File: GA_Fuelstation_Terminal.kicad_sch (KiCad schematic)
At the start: 0 parts

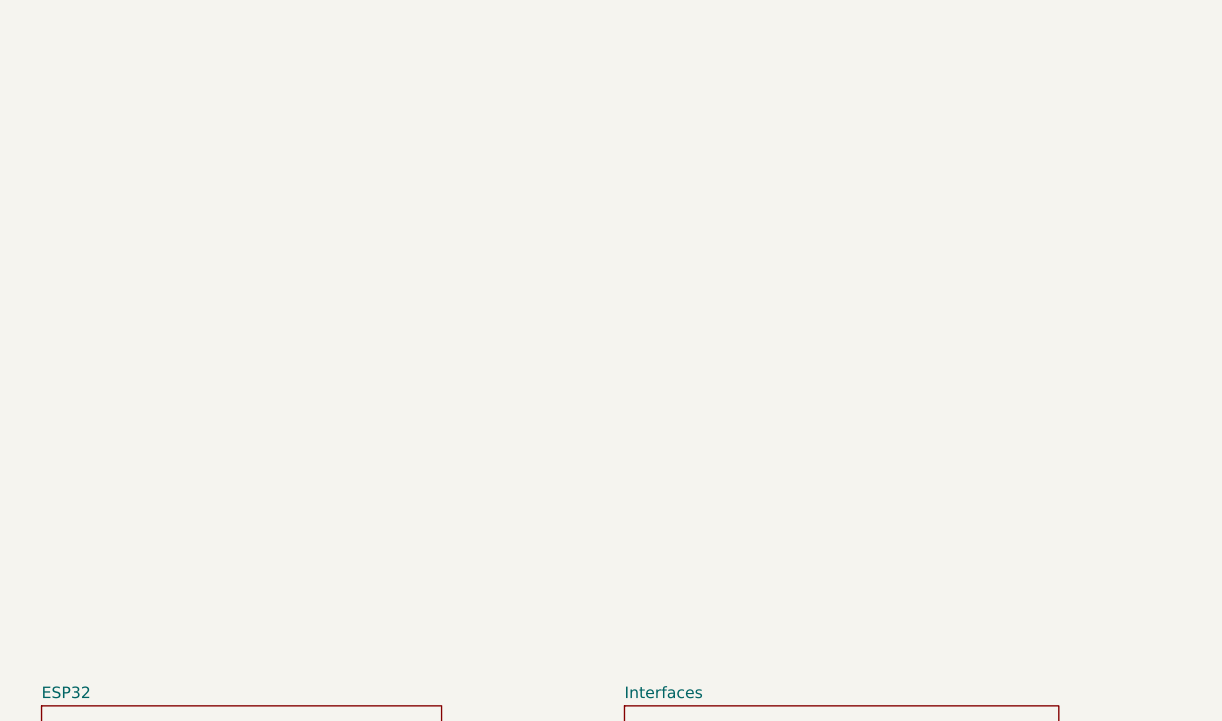
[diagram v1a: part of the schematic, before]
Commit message: Adapted gitignore Add LAN Add USB2RS232
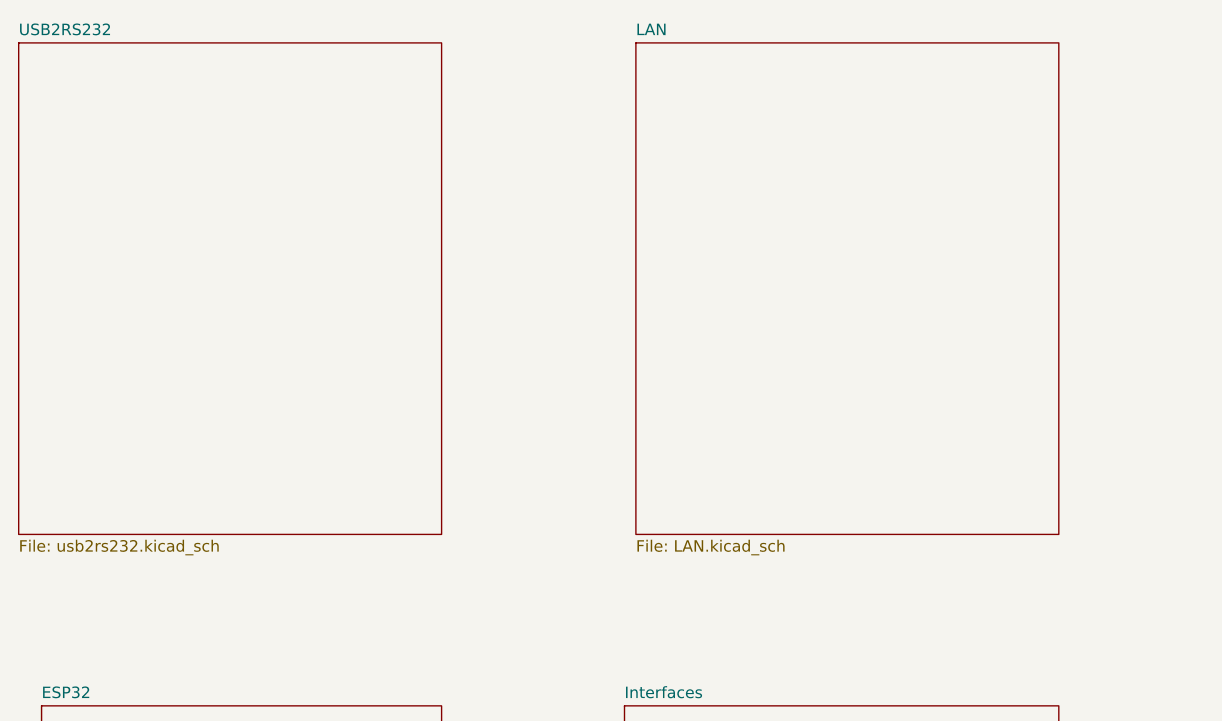
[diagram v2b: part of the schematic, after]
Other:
- added sheet LAN (LAN.kicad_sch)
- added sheet USB2RS232 (usb2rs232.kicad_sch)
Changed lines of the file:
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@@
+	)
+	(sheet
+		(at 99.06 38.1)
+		(size 46.99 54.61)
+		(exclude_from_sim no)
+		(in_bom yes)
+		(on_board yes)
+		(dnp no)
+		(fields_autoplaced yes)
+		(stroke
+			(width 0.1524)
+			(type solid)
+		)
+		(fill
+			(color 0 0 0 0)
+		)
+		(property "Sheetname" "LAN"
+			(at 99.06 37.3884 0)
+			(show_name no)
+			(do_not_autoplace no)
+			(effects
+				(font
+					(size 1.27 1.27)
+				)
+				(justify left bottom)
+			)
+		)
+		(property "Sheetfile" "LAN.kicad_sch"
+			(at 99.06 93.2946 0)
+			(show_name no)
+			(do_not_autoplace no)
+			(effects
+				(font
+					(size 1.27 1.27)
+				)
+				(justify left top)
+			)
+		)
+		(instances
+			(project "GA_Fuelstation_Terminal"
+				(path "/9d5c9b65-fa9a-4f2b-b8e4-a4447f224f28"
+					(page "5")
+				)
+			)
+		)
 	)
 	(sheet
@@
 				)
 			)
+		)
+	)
+	(sheet
+		(at 30.48 38.1)
+		(size 46.99 54.61)
+		(exclude_from_sim no)
+		(in_bom yes)
+		(on_board yes)
+		(dnp no)
+		(fields_autoplaced yes)
+		(stroke
+			(width 0.1524)
+			(type solid)
+		)
+		(fill
+			(color 0 0 0 0)
+		)
+		(property "Sheetname" "USB2RS232"
+			(at 30.48 37.3884 0)
+			(show_name no)
+			(do_not_autoplace no)
+			(effects
+				(font
+					(size 1.27 1.27)
+				)
+				(justify left bottom)
+			)
+		)
+		(property "Sheetfile" "usb2rs232.kicad_sch"
+			(at 30.48 93.2946 0)
+			(show_name no)
+			(do_not_autoplace no)
+			(effects
+				(font
+					(size 1.27 1.27)
+				)
+				(justify left top)
+			)
+		)
+		(instances
+			(project "GA_Fuelstation_Terminal"
+				(path "/9d5c9b65-fa9a-4f2b-b8e4-a4447f224f28"
+					(page "6")
+				)
+			)
